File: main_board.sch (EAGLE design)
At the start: 107 parts, among them IC1 MBED_MICROCONTROLLER, M1_1 M01_WIRE, M1_10 M01_WIRE, M1_11 M01_WIRE, M1_12 M01_WIRE, M1_2 M01_WIRE, M1_3 M01_WIRE, M1_4 M01_WIRE, M1_5 M01_WIRE, M1_6 M01_WIRE, M1_7 M01_WIRE, M1_8 M01_WIRE, M1_9 M01_WIRE, U1 PCA9555PW,118, U11 MC33887-HSOP, U13 MC33887-HSOP, U2 SI8460AA-B-IS1, U3 MC33887-HSOP, U6 SI8460AA-B-IS1, U7 MC33887-HSOP, U8 SI8460AA-B-IS1, U9 MC33887-HSOP, X1 BALL_SENS, X10 IMU, X2 ETH, X3 ENC1, X4 ENC2, X5 BTNS, X6 ENC3, X7 ENC4, X8 ENC5, X9 COIL

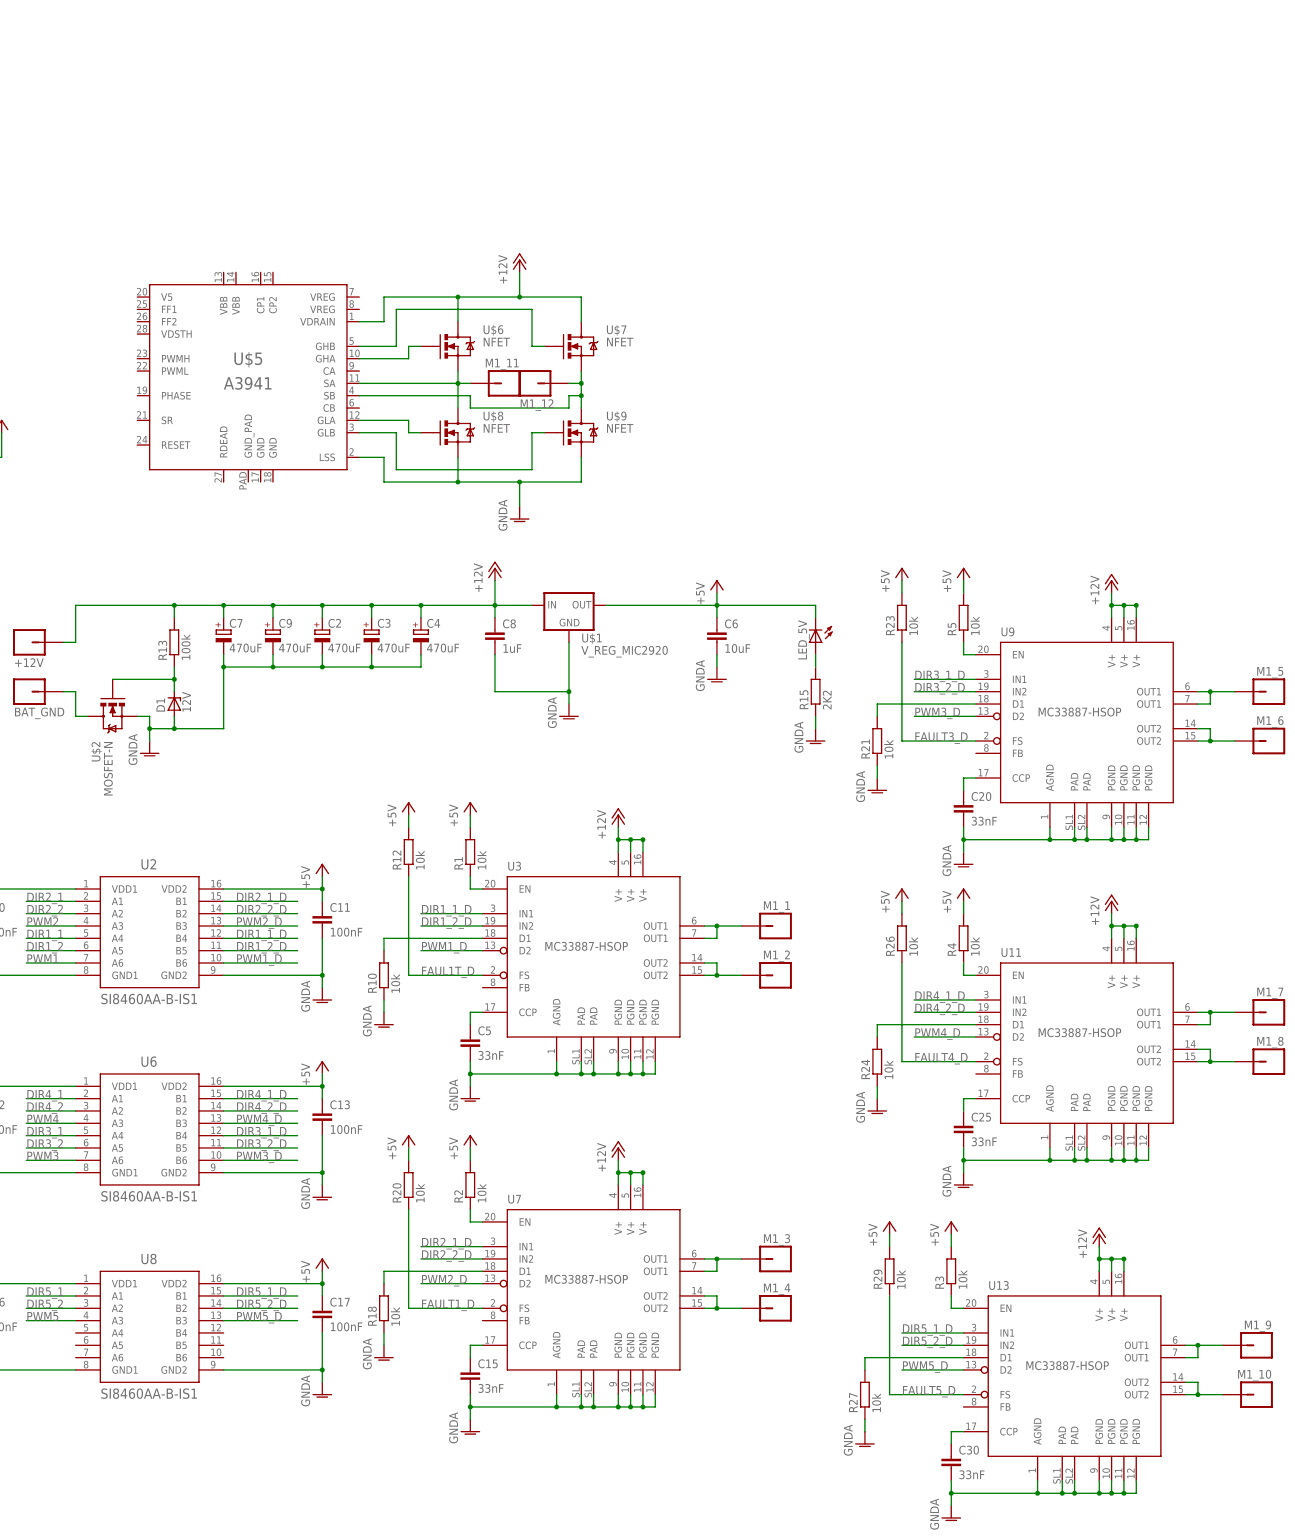
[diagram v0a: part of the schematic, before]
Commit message: Added one driver module
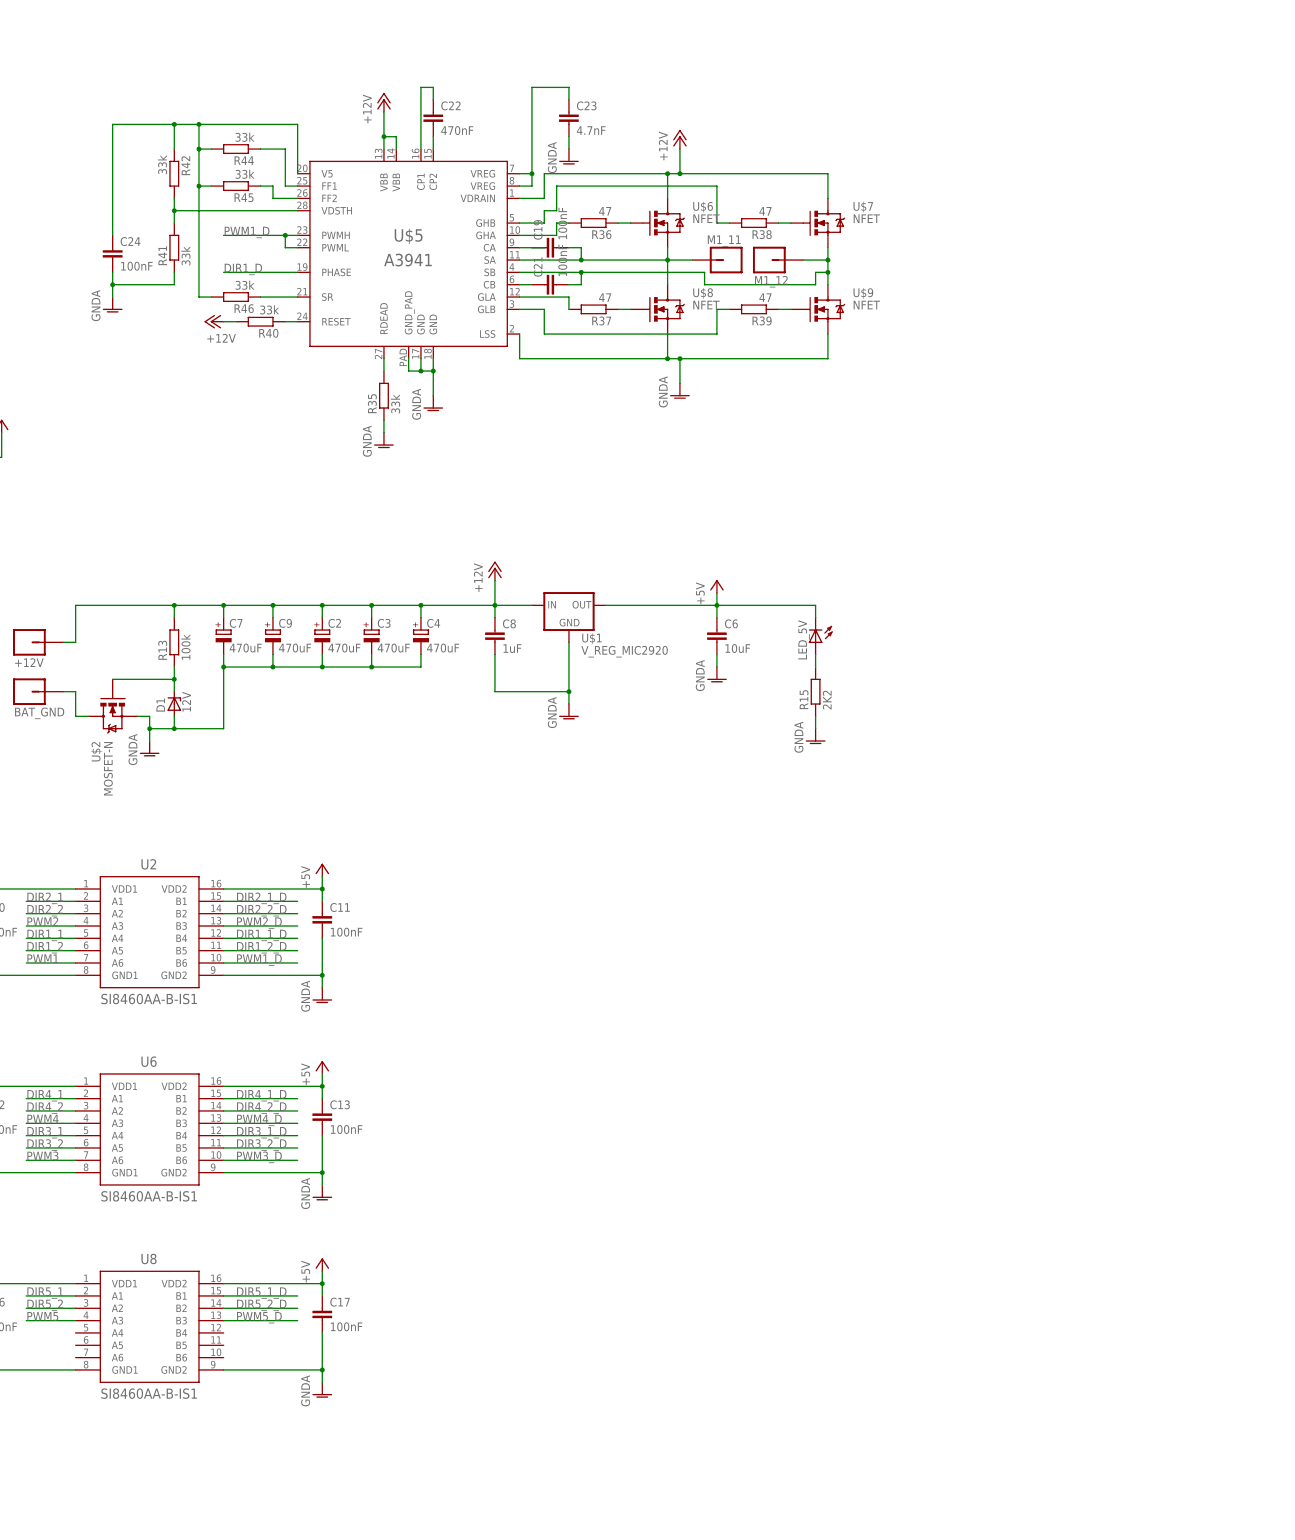
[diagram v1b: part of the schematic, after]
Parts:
- removed C15, C20, C25, C30, C5: 33nF, rcl:C-EUC0603K
- removed M1_1, M1_10, M1_2, M1_3, M1_4, M1_5, M1_6, M1_7, M1_8, M1_9: M01_WIRE, tellis2:M01_WIRE
- removed R1, R10, R12, R18, R2, R20, R21, R23, R24, R26, R27, R29, R3, R4, R5: 10k, rcl:R-EU_R0603
- removed U11, U13, U3, U7, U9: MC33887-HSOP, mc33887:MC33887-HSOP
- added C19, C21, C24: 100nF, rcl:C-EUC0603K
- added C22: 470nF, rcl:C-EUC1206K
- added C23: 4.7nF, rcl:C-EUC1206K
- added R35, R40, R41, R42, R44, R45, R46: 33k, rcl:R-EU_R0603
- added R36, R37, R38, R39: 47, rcl:R-EU_R0603
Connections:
- removed net FAUL1T_D: R12.1, U3.FS
- removed net FAULT1_D: R20.1, U7.FS
- removed net FAULT3_D: R23.1, U9.FS
- removed net FAULT4_D: R26.1, U11.FS
- removed net FAULT5_D: R29.1, U13.FS
- removed net N$15: C5.1, U3.CCP
- removed net N$18: R10.2, U3.D1
- removed net N$2: R1.1, U3.EN
- removed net N$23: M1_1.P$1, U3.OUT1, U3.OUT1@1
- removed net N$25: M1_2.P$1, U3.OUT2, U3.OUT2@1
- removed net N$3: R2.1, U7.EN
- removed net N$31: C15.1, U7.CCP
- removed net N$33: R18.2, U7.D1
- removed net N$34: M1_3.P$1, U7.OUT1, U7.OUT1@1
- removed net N$35: M1_4.P$1, U7.OUT2, U7.OUT2@1
- removed net N$36: C20.1, U9.CCP
- removed net N$38: R21.2, U9.D1
- removed net N$39: M1_5.P$1, U9.OUT1, U9.OUT1@1
- removed net N$4: R3.1, U13.EN
- removed net N$40: M1_6.P$1, U9.OUT2, U9.OUT2@1
- removed net N$41: C25.1, U11.CCP
- removed net N$43: R24.2, U11.D1
- removed net N$44: M1_7.P$1, U11.OUT1, U11.OUT1@1
- removed net N$45: M1_8.P$1, U11.OUT2, U11.OUT2@1
- removed net N$46: C30.1, U13.CCP
- removed net N$48: R27.2, U13.D1
- removed net N$49: M1_9.P$1, U13.OUT1, U13.OUT1@1
- removed net N$5: R4.1, U11.EN
- removed net N$50: M1_10.P$1, U13.OUT2, U13.OUT2@1
- removed net N$6: R5.1, U9.EN
- new net DIR1_D: U$5.PHASE
- new net N$19: C21.1, U$5.CB
- new net N$26: C19.1, U$5.CA
- new net N$27: R35.2, U$5.RDEAD
- new net N$28: R36.2, U$5.GHA
- new net N$29: R38.2, U$5.GHB
- new net N$30: R37.2, U$5.GLA
- new net N$32: R39.2, U$5.GLB
- new net N$37: C22.1, U$5.CP1
- new net N$42: C22.2, U$5.CP2
- new net N$47: C23.1, U$5.VREG@7, U$5.VREG@8
- new net N$51: R41.2, R42.2, U$5.VDSTH
- new net N$52: C24.1, R42.1, R44.2, R45.2, R46.2, U$5.V5
- new net N$53: R45.1, U$5.FF2
- new net N$54: R40.1, U$5.RESET
- new net N$55: R44.1, U$5.FF1
- new net N$59: R46.1, U$5.SR
- net +12V: now also R40.2, U$5.VBB@13, U$5.VBB@14; no longer U11.V+, U11.V+@1, U11.V+@2, U13.V+, U13.V+@1, U13.V+@2, U3.V+, U3.V+@1, U3.V+@2, U7.V+, U7.V+@1, U7.V+@2, U9.V+, U9.V+@1, U9.V+@2
- net +5V: no longer R1.2, R12.2, R2.2, R20.2, R23.2, R26.2, R29.2, R3.2, R4.2, R5.2
- net DIR1_1_D: no longer U3.IN1
- net DIR1_2_D: no longer U3.IN2
- net DIR2_1_D: no longer U7.IN1
- net DIR2_2_D: no longer U7.IN2
- net DIR3_1_D: no longer U9.IN1
- net DIR3_2_D: no longer U9.IN2
- net DIR4_1_D: no longer U11.IN1
- net DIR4_2_D: no longer U11.IN2
- net DIR5_1_D: no longer U13.IN1
- net DIR5_2_D: no longer U13.IN2
- net GNDA: now also C23.2, C24.2, R35.1, R41.1, U$5.GND@17, U$5.GND@18, U$5.GND_PAD; no longer C15.2, C20.2, C25.2, C30.2, C5.2, R10.1, R18.1, R21.1, R24.1, R27.1, U11.AGND, U11.PAD, U11.PAD@1, U11.PGND, U11.PGND@1, U11.PGND@2, U11.PGND@3, U13.AGND, U13.PAD, U13.PAD@1, U13.PGND, U13.PGND@1, U13.PGND@2, U13.PGND@3, U3.AGND, U3.PAD, U3.PAD@1, U3.PGND, U3.PGND@1, U3.PGND@2, U3.PGND@3, U7.AGND, U7.PAD, U7.PAD@1, U7.PGND, U7.PGND@1, U7.PGND@2, U7.PGND@3, U9.AGND, U9.PAD, U9.PAD@1, U9.PGND, U9.PGND@1, U9.PGND@2, U9.PGND@3
- net N$13: now also R37.1, U$8.G; no longer U$5.GHA, U$6.G
- net N$14: now also R38.1; no longer U$5.GHB
- net N$16: now also R39.1, U$9.G; no longer U$5.GLA, U$8.G
- net N$17: now also R36.1, U$6.G; no longer U$5.GLB, U$9.G
- net N$22: now also C19.2
- net N$24: now also C21.2
- net PWM1_D: now also U$5.PWMH, U$5.PWML; no longer U3.D2
- net PWM2_D: no longer U7.D2
- net PWM3_D: no longer U9.D2
- net PWM4_D: no longer U11.D2
- net PWM5_D: no longer U13.D2
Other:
- moved on the sheet: M1_11, M1_12, U$5, U$6, U$7, U$8, U$9
